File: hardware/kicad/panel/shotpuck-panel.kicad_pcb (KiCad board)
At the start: 2 copper layers, 75 x 91 mm, 237 parts, among them J1_0 Samzo PR5L4015-2P-C-F, J1_1 Samzo PR5L4015-2P-C-F, J1_2 Samzo PR5L4015-2P-C-F, J1_3 Samzo PR5L4015-2P-C-F, J2_0 TC2030-NL, J2_1 TC2030-NL, J2_2 TC2030-NL, J2_3 TC2030-NL, Q1_0 DMN63D8LDW, Q1_1 DMN63D8LDW, Q1_2 DMN63D8LDW, Q1_3 DMN63D8LDW, Q2_0 DMN2004DWK, Q2_1 DMN2004DWK, Q2_2 DMN2004DWK, Q2_3 DMN2004DWK, U1_0 MDBT50Q-1MV2, U1_1 MDBT50Q-1MV2, U1_2 MDBT50Q-1MV2, U1_3 MDBT50Q-1MV2, U2_0 LSM6DSO32TR, U2_1 LSM6DSO32TR, U2_2 LSM6DSO32TR, U2_3 LSM6DSO32TR, U3_0 MCP73831T-2ACI/OT, U3_1 MCP73831T-2ACI/OT, U3_2 MCP73831T-2ACI/OT, U3_3 MCP73831T-2ACI/OT, U4_0 BQ29700DSER, U4_1 BQ29700DSER, U4_2 BQ29700DSER, U4_3 BQ29700DSER

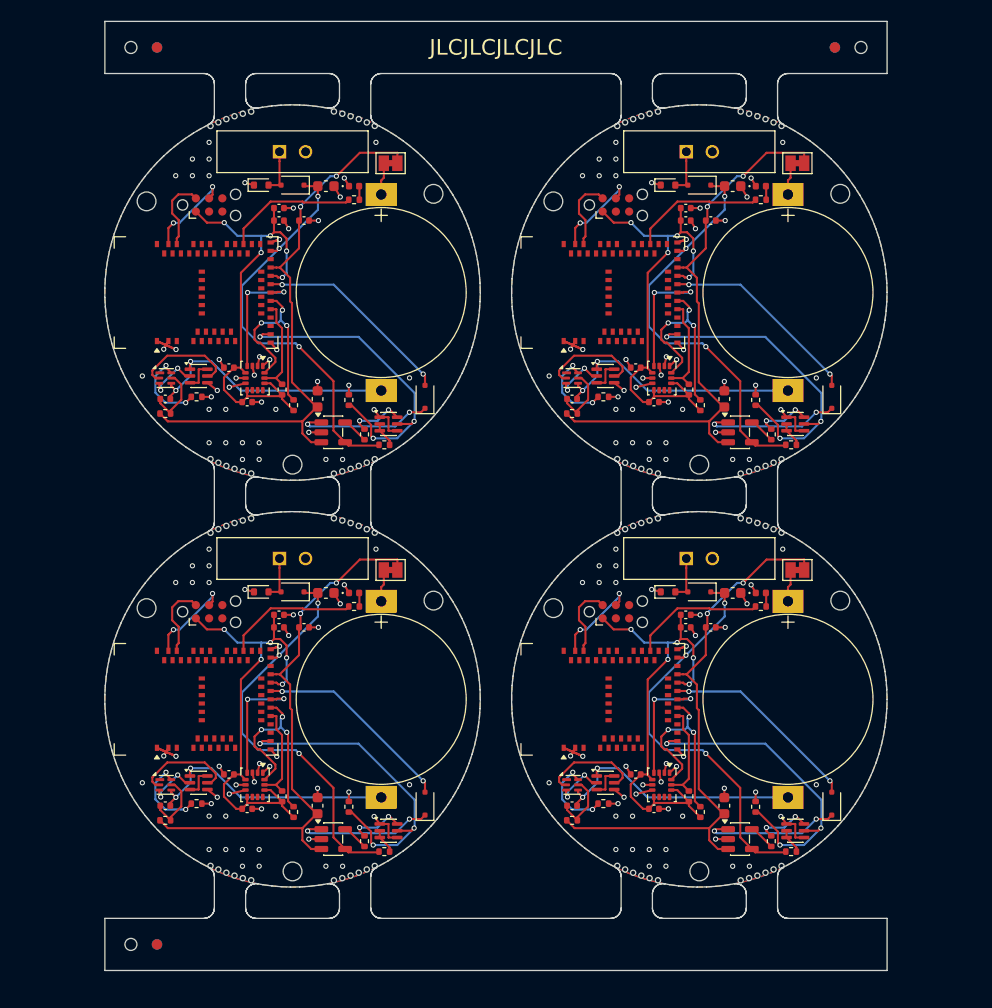
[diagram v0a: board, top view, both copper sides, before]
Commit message: Seat the cell in a PCB notch open to the rim (puck 10.45 mm)
- The cell sits on the Kapton over the base in a notch in the PCB
  (Ø16.6 mm round end, open to the rim) instead of on top of the board,
  saving the 0.8 mm board thickness: 11.25 -> 10.45 mm, 19.8 g with the
  optional brass pins, 18.0 g without.
- Rounded relief on the + side lets the bottom (+ can) tab bend up to the
  + pad; cell pads moved to ±10.2 mm.
- Screw boss 35° -> 40° so its face stays on the board beside the notch;
  JP1 turned upright, D2 moved to the bottom centre (CHG_STAT had no route
  past the notch).
- gen_pcb.py builds the whole outline (rim arc, notch lines, arcs) and a
  copper keep-out along the notch; puck.py cuts the same shape.
- Assembly: full Kapton disc, foam/RTV between cell and cap wall.
- Board DRC 0/0, panel DRC 0/0, netlist PASS; fab, panel and JLC files
  regenerated.

Co-Authored-By: Claude Opus 5.5 <noreply@anthropic.com>
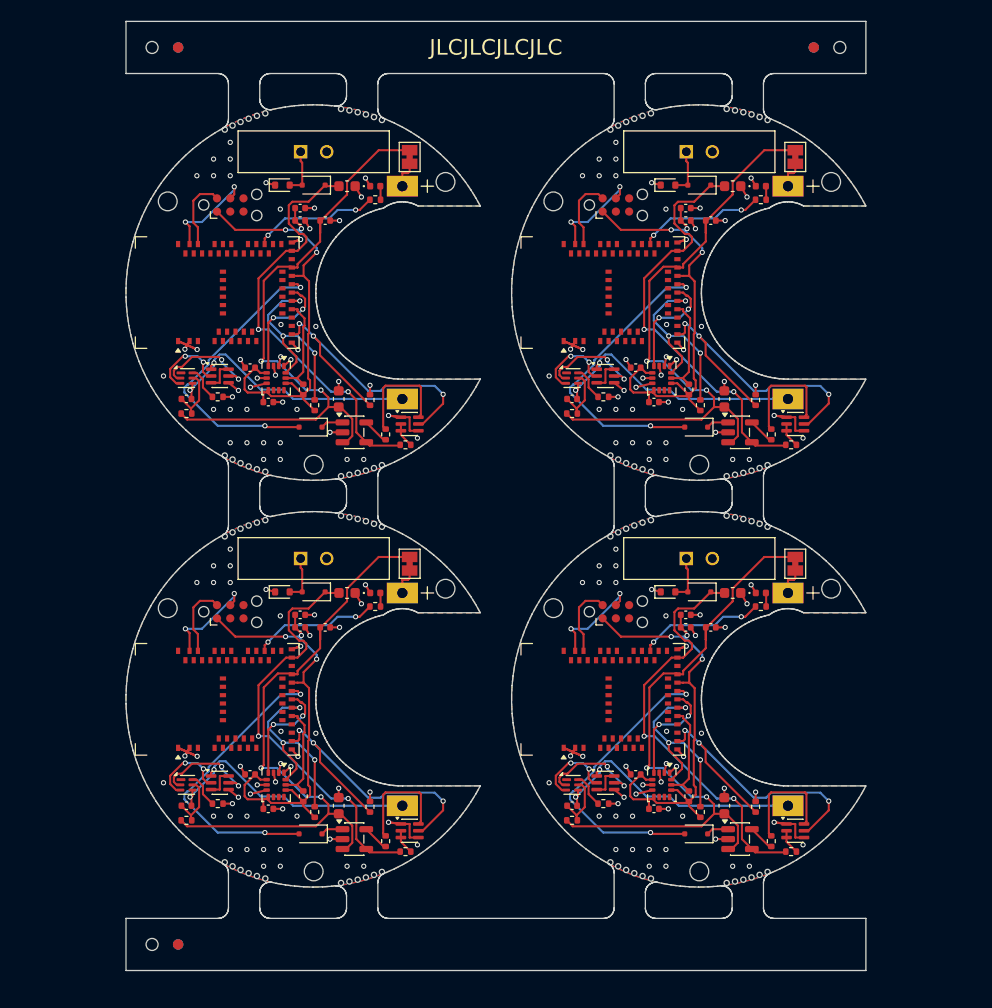
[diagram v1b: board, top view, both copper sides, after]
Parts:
- moved D2_3 13.3 mm to (167.7, 97.9), turned to 180 degrees
- moved D2_1 13.3 mm to (167.7, 58.9), turned to 180 degrees
- moved D2_2 11.3 mm to (130.7, 97.9), turned to 180 degrees
- moved D2_0 11.3 mm to (130.7, 58.9), turned to 180 degrees
- moved KiKit_FID_B_3 2.03 mm to (118.0, 108.5)
- moved KiKit_FID_T_3 2.03 mm to (118.0, 108.5)
- moved KiKit_TO_3 2.03 mm to (115.5, 108.5)
- moved KiKit_FID_B_2 2.03 mm to (179.0, 22.5)
- moved KiKit_FID_T_2 2.03 mm to (179.0, 22.5)
- moved KiKit_TO_2 2.03 mm to (181.5, 22.5)
- moved KiKit_FID_B_1 2.03 mm to (118.0, 22.5)
- moved KiKit_FID_T_1 2.03 mm to (118.0, 22.5)
- moved KiKit_TO_1 2.03 mm to (115.5, 22.5)
- moved BT1_0 2.03 mm to (139.5, 46.0)
- moved BT1_2 2.03 mm to (139.5, 85.0)
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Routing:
- net Board_1-STAT: track 13.4 -> 2.15 mm, vias 2 -> 0
- net Board_0-STAT: track 13.4 -> 2.15 mm, vias 2 -> 0
- net Board_3-STAT: track 13.4 -> 2.15 mm, vias 2 -> 0
- net Board_2-STAT: track 13.4 -> 2.15 mm, vias 2 -> 0
- net Board_3-CHG_STAT: track 19.3 -> 29.2 mm
- net Board_1-CHG_STAT: track 19.3 -> 29.2 mm
- net Board_2-CHG_STAT: track 19.3 -> 29.2 mm
- net Board_0-CHG_STAT: track 19.3 -> 29.2 mm
- net Board_3-PROG_SW: track 5.32 -> 10.8 mm, vias 2 -> 0
- net Board_2-PROG_SW: track 5.32 -> 10.8 mm, vias 2 -> 0
- net Board_1-PROG_SW: track 5.32 -> 10.8 mm, vias 2 -> 0
- net Board_0-PROG_SW: track 5.32 -> 10.8 mm, vias 2 -> 0
- net Board_3-VBAT: track 54.2 -> 59.5 mm
- net Board_1-VBAT: track 54.2 -> 59.5 mm
- net Board_0-VBAT: track 54.2 -> 59.5 mm
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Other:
- board size 75 x 91 mm -> 70.9 x 91 mm

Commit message: Update ShotPuck design to rev A: replace stud with flat plate, adjust dimensions, and enhance PCB layout
- Redesigned the ShotPuck to use a 2.0 mm flat 6061 plate, bolted through a steel sleeve, improving manufacturability and cost.
- Adjusted dimensions: puck height reduced to 9.90 mm, with a center of mass 0.85 mm off-axis.
- Updated layout.json to reflect new design parameters, including cell placement and PCB notch.
- Enhanced mechanical and electrical design files, including updated battery specifications (LIR1254) and revised component placements.
- Improved documentation in HANDOVER.md and README.md to reflect changes in design and functionality.

Co-Authored-By: Claude Opus 5.5 <noreply@anthropic.com>
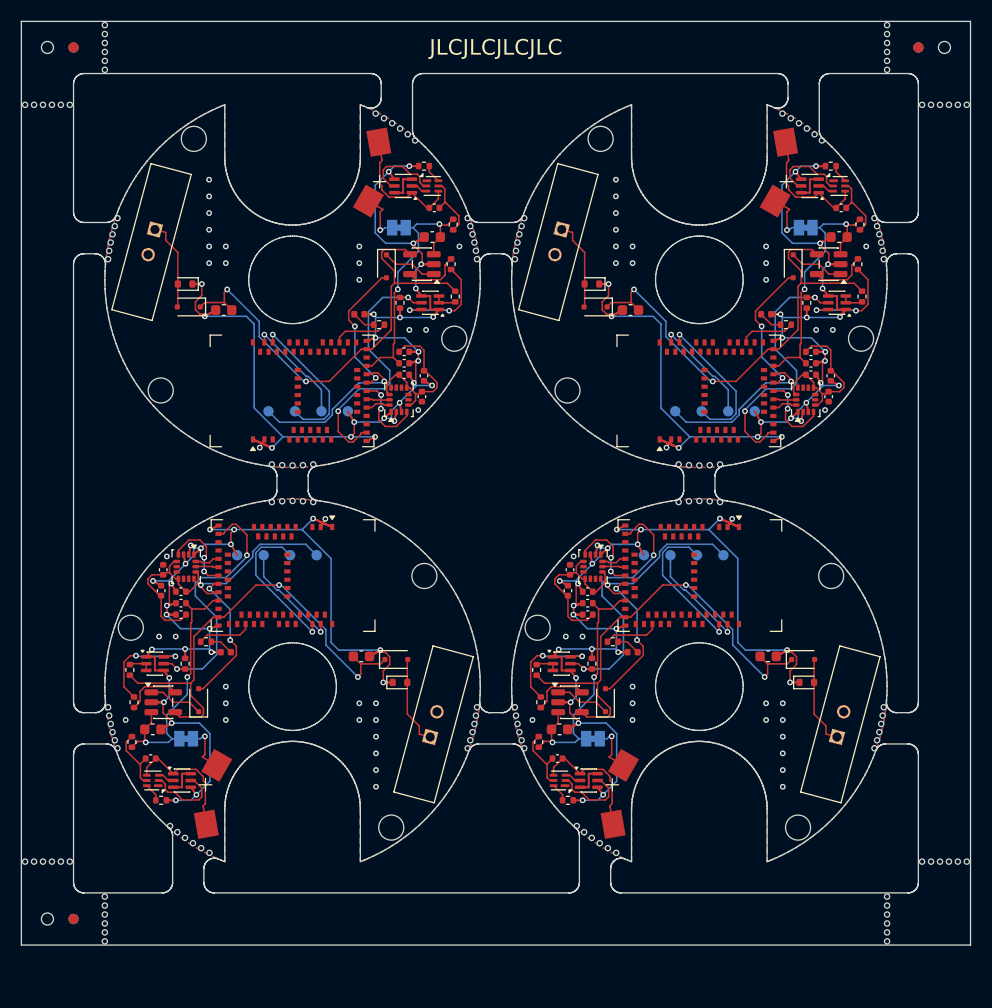
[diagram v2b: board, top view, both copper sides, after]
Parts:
- removed KiKit_MB_10_6, KiKit_MB_14_6, KiKit_MB_2_6, KiKit_MB_6_6: NPTH, NPTH
- removed R5_0, R5_1, R5_2, R5_3, R6_0, R6_1, R6_2, R6_3: 4.7k DNP, Resistor_SMD:R_0402_1005Metric
- added KiKit_MB_17_2: NPTH, NPTH, F.Cu at (111.0, 20.4)
- added KiKit_MB_17_3: NPTH, NPTH, F.Cu at (111.0, 21.2)
- added KiKit_MB_17_4: NPTH, NPTH, F.Cu at (111.0, 22.1)
- added KiKit_MB_17_5: NPTH, NPTH, F.Cu at (111.0, 22.9)
- added KiKit_MB_17_6: NPTH, NPTH, F.Cu at (111.0, 23.8)
- added KiKit_MB_17_7: NPTH, NPTH, F.Cu at (111.0, 24.6)
- added KiKit_MB_18_2: NPTH, NPTH, F.Cu at (186.0, 20.4)
- added KiKit_MB_18_3: NPTH, NPTH, F.Cu at (186.0, 21.2)
- added KiKit_MB_18_4: NPTH, NPTH, F.Cu at (186.0, 22.1)
- added KiKit_MB_18_5: NPTH, NPTH, F.Cu at (186.0, 22.9)
- added KiKit_MB_18_6: NPTH, NPTH, F.Cu at (186.0, 23.8)
- added KiKit_MB_18_7: NPTH, NPTH, F.Cu at (186.0, 24.6)
- added KiKit_MB_19_2: NPTH, NPTH, F.Cu at (111.0, 103.9)
- added KiKit_MB_19_3: NPTH, NPTH, F.Cu at (111.0, 104.8)
- added KiKit_MB_19_4: NPTH, NPTH, F.Cu at (111.0, 105.6)
- added KiKit_MB_19_5: NPTH, NPTH, F.Cu at (111.0, 106.5)
- added KiKit_MB_19_6: NPTH, NPTH, F.Cu at (111.0, 107.3)
- added KiKit_MB_19_7: NPTH, NPTH, F.Cu at (111.0, 108.2)
- added KiKit_MB_20_2: NPTH, NPTH, F.Cu at (186.0, 103.9)
- added KiKit_MB_20_3: NPTH, NPTH, F.Cu at (186.0, 104.8)
- added KiKit_MB_20_4: NPTH, NPTH, F.Cu at (186.0, 105.6)
- added KiKit_MB_20_5: NPTH, NPTH, F.Cu at (186.0, 106.5)
- added KiKit_MB_20_6: NPTH, NPTH, F.Cu at (186.0, 107.3)
- added KiKit_MB_20_7: NPTH, NPTH, F.Cu at (186.0, 108.2)
- added KiKit_MB_21_2: NPTH, NPTH, F.Cu at (103.4, 28.0)
- added KiKit_MB_21_3: NPTH, NPTH, F.Cu at (104.2, 28.0)
- added KiKit_MB_21_4: NPTH, NPTH, F.Cu at (105.1, 28.0)
- added KiKit_MB_21_5: NPTH, NPTH, F.Cu at (105.9, 28.0)
- added KiKit_MB_21_6: NPTH, NPTH, F.Cu at (106.8, 28.0)
- added KiKit_MB_21_7: NPTH, NPTH, F.Cu at (107.6, 28.0)
- added KiKit_MB_22_2: NPTH, NPTH, F.Cu at (103.4, 100.6)
- added KiKit_MB_22_3: NPTH, NPTH, F.Cu at (104.2, 100.6)
- added KiKit_MB_22_4: NPTH, NPTH, F.Cu at (105.1, 100.6)
- added KiKit_MB_22_5: NPTH, NPTH, F.Cu at (105.9, 100.6)
- added KiKit_MB_22_6: NPTH, NPTH, F.Cu at (106.8, 100.6)
- added KiKit_MB_22_7: NPTH, NPTH, F.Cu at (107.6, 100.6)
- added KiKit_MB_23_2: NPTH, NPTH, F.Cu at (189.4, 28.0)
- added KiKit_MB_23_3: NPTH, NPTH, F.Cu at (190.2, 28.0)
- added KiKit_MB_23_4: NPTH, NPTH, F.Cu at (191.1, 28.0)
- added KiKit_MB_23_5: NPTH, NPTH, F.Cu at (191.9, 28.0)
- added KiKit_MB_23_6: NPTH, NPTH, F.Cu at (192.8, 28.0)
- added KiKit_MB_23_7: NPTH, NPTH, F.Cu at (193.6, 28.0)
- added KiKit_MB_24_2: NPTH, NPTH, F.Cu at (189.4, 100.6)
- added KiKit_MB_24_3: NPTH, NPTH, F.Cu at (190.2, 100.6)
- added KiKit_MB_24_4: NPTH, NPTH, F.Cu at (191.1, 100.6)
- added KiKit_MB_24_5: NPTH, NPTH, F.Cu at (191.9, 100.6)
- added KiKit_MB_24_6: NPTH, NPTH, F.Cu at (192.8, 100.6)
- added KiKit_MB_24_7: NPTH, NPTH, F.Cu at (193.6, 100.6)
- BT1_0, BT1_1, BT1_2, BT1_3: value Varta CP1654 A3 (wire or tag version) -> LIR1254 (plain, spring contacts); footprint ShotPuck:CP1654_Pads -> ShotPuck:LIR1254_Contacts
- H1_0, H1_1, H1_2, H1_3, H2_0, H2_1, H2_2, H2_3, H3_0, H3_1, H3_2, H3_3: value M1.6 -> M2; footprint ShotPuck:MountingHole_1.8mm_NPTH -> ShotPuck:MountingHole_2.4mm_NPTH
- J2_0, J2_1, J2_2, J2_3: value TC2030-NL -> SWD pads; footprint Connector:Tag-Connect_TC2030-IDC-NL_2x03_P1.27mm_Vertical -> ShotPuck:SWD_Pads_1x4_P2.54; moved to B.Cu
- JP1_0, JP1_1, JP1_2, JP1_3: moved to B.Cu
- R1_0, R1_1, R1_2, R1_3: value 20k 1% -> 47k 1%
- moved KiKit_MB_2_5 34.7 mm to (127.0, 62.5)
- moved KiKit_MB_2_4 34.6 mm to (128.0, 62.5)
- moved KiKit_MB_2_3 34.4 mm to (129.0, 62.6)
- moved KiKit_MB_2_2 34.3 mm to (130.0, 62.5)
- moved KiKit_MB_6_5 34.2 mm to (166.0, 62.5)
- moved KiKit_MB_2_1 34.2 mm to (131.0, 62.5)
- moved KiKit_MB_6_4 34.2 mm to (167.0, 62.5)
- moved KiKit_MB_6_3 34.1 mm to (168.0, 62.6)
- moved KiKit_MB_6_2 34.1 mm to (169.0, 62.5)
- moved KiKit_MB_6_1 34.1 mm to (170.0, 62.5)
- moved H1_0 33.8 mm to (116.4, 55.4), turned to 180 degrees
- moved H3_0 33.3 mm to (119.5, 31.3), turned to 180 degrees
- moved R7_1 33.0 mm to (183.4, 39.5), turned to -90 degrees
- moved H3_1 32.6 mm to (158.5, 31.3), turned to 180 degrees
- moved H2_1 32.3 mm to (183.5, 50.4), turned to 180 degrees
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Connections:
- J2_0 pad 3: (no net) -> Board_0-SWDCLK
- J2_0 pad 4: Board_0-SWDCLK -> Board_0-GND
- J2_1 pad 3: (no net) -> Board_1-SWDCLK
- J2_1 pad 4: Board_1-SWDCLK -> Board_1-GND
- J2_2 pad 3: (no net) -> Board_2-SWDCLK
- J2_2 pad 4: Board_2-SWDCLK -> Board_2-GND
- J2_3 pad 3: (no net) -> Board_3-SWDCLK
- J2_3 pad 4: Board_3-SWDCLK -> Board_3-GND
- U1_0 pad 20: Board_0-SCL -> Board_0-SDA
- U1_0 pad 22: Board_0-SDA -> Board_0-SCL
- U1_1 pad 20: Board_1-SCL -> Board_1-SDA
- U1_1 pad 22: Board_1-SDA -> Board_1-SCL
- U1_2 pad 20: Board_2-SCL -> Board_2-SDA
- U1_2 pad 22: Board_2-SDA -> Board_2-SCL
- U1_3 pad 20: Board_3-SCL -> Board_3-SDA
- U1_3 pad 22: Board_3-SDA -> Board_3-SCL
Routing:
- net Board_1-GND: track 31.7 -> 109.5 mm, vias 46 -> 38
- net Board_3-GND: track 31.7 -> 109.5 mm, vias 46 -> 38
- net Board_2-GND: track 31.7 -> 109.5 mm, vias 46 -> 38
- net Board_0-GND: track 31.7 -> 109.5 mm, vias 46 -> 38
- net Board_3-VBAT: track 59.5 -> 25.4 mm
- net Board_1-VBAT: track 59.5 -> 25.4 mm
- net Board_0-VBAT: track 59.5 -> 25.4 mm
- net Board_2-VBAT: track 59.5 -> 25.4 mm
- net Board_3-SDA: track 19.7 -> 2.39 mm, vias 3 -> 0
- net Board_1-SDA: track 19.7 -> 2.39 mm, vias 3 -> 0
- net Board_2-SDA: track 19.7 -> 2.39 mm, vias 3 -> 0
- net Board_0-SDA: track 19.7 -> 2.39 mm, vias 3 -> 0
- net Board_3-CHG_STAT: track 29.2 -> 13.5 mm
- net Board_1-CHG_STAT: track 29.2 -> 13.5 mm
- net Board_0-CHG_STAT: track 29.2 -> 13.5 mm
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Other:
- board size 70.9 x 91 mm -> 91 x 88.6 mm

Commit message: Refine ShotPuck design and documentation for improved functionality and clarity
- Updated `HANDOVER.md` to clarify PCB routing and placement procedures, emphasizing the importance of running `gen_pcb.py --no-route` and `global_route.py` for optimal results.
- Revised `README.md` to correct the center of mass measurement and enhance the description of the puck's dimensions.
- Enhanced `VALIDATION.md` to reflect updated weight and balance metrics, ensuring accurate representation of the ShotPuck's specifications.
- Adjusted `design.py` to include new charge-input protection details and updated component specifications for better clarity.
- Improved `gen_bom.py` and `gen_jlc.py` to reflect changes in component sourcing and specifications.

Co-Authored-By: Claude Opus 5.5 <noreply@anthropic.com>
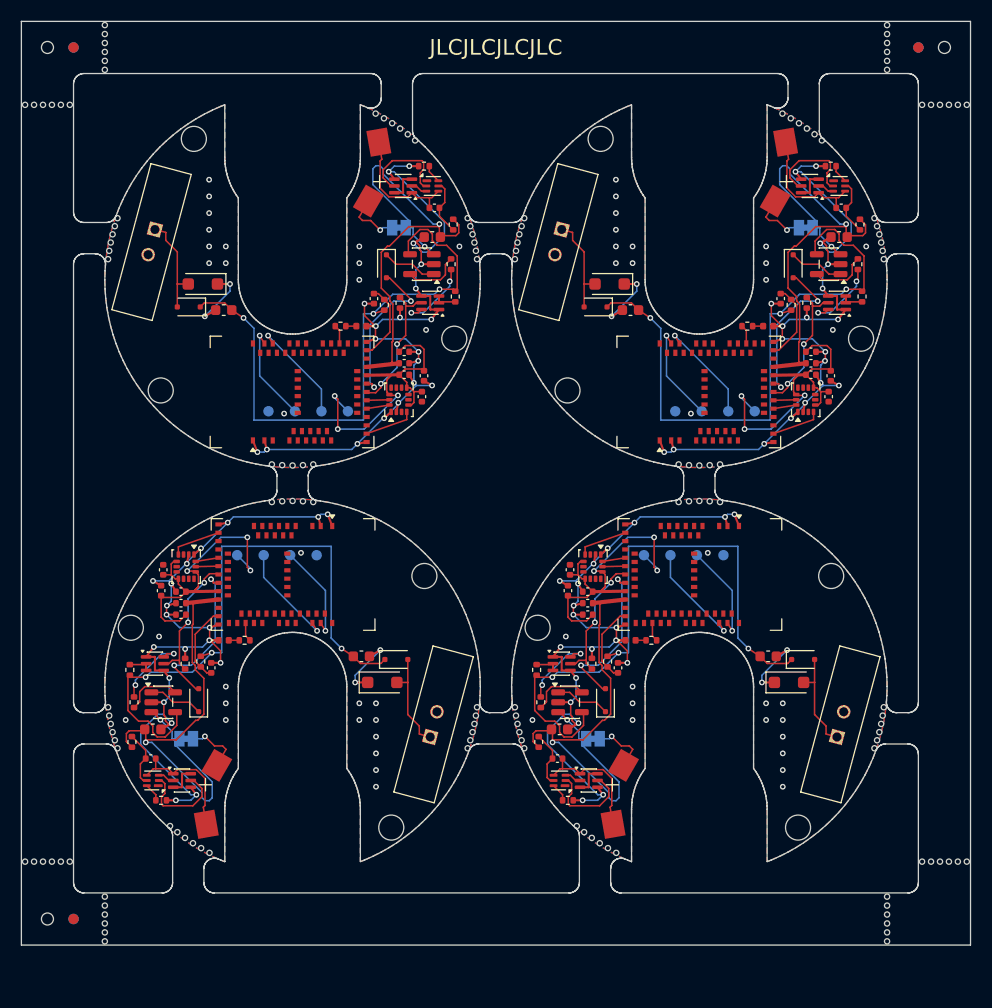
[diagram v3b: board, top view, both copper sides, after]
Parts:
- added C9_0: 100n, Capacitor_SMD:C_0402_1005Metric, F.Cu at (136.8, 46.6)
- added C9_1: 100n, Capacitor_SMD:C_0402_1005Metric, F.Cu at (175.8, 46.6)
- added C9_2: 100n, Capacitor_SMD:C_0402_1005Metric, F.Cu at (121.2, 82.0)
- added C9_3: 100n, Capacitor_SMD:C_0402_1005Metric, F.Cu at (160.2, 82.0)
- added R9_0: 1k, Resistor_SMD:R_0402_1005Metric, F.Cu at (137.8, 47.2)
- added R9_1: 1k, Resistor_SMD:R_0402_1005Metric, F.Cu at (176.8, 47.2)
- added R9_2: 1k, Resistor_SMD:R_0402_1005Metric, F.Cu at (120.2, 81.4)
- added R9_3: 1k, Resistor_SMD:R_0402_1005Metric, F.Cu at (159.2, 81.4)
- C2_0, C2_1, C2_2, C2_3: value 4.7u 10V -> 10u 10V
- D3_0, D3_1, D3_2, D3_3: value PESD5V0S1BB -> SMF5.0CA; footprint Diode_SMD:D_SOD-523 -> Diode_SMD:D_SOD-123F
- D4_0, D4_1, D4_2, D4_3: value LED green 0402 -> LED yellow-green 0402
- moved KiKit_MB_15_3 34.7 mm to (150.7, 88.1)
- moved KiKit_MB_15_4 34.7 mm to (150.6, 87.4)
- moved KiKit_MB_16_3 34.7 mm to (185.4, 87.4)
- moved KiKit_MB_16_4 34.7 mm to (185.3, 88.1)
- moved KiKit_MB_7_3 34.7 mm to (185.3, 40.4)
- moved KiKit_MB_7_4 34.7 mm to (185.4, 41.2)
- moved KiKit_MB_8_3 34.7 mm to (150.6, 41.2)
- moved KiKit_MB_8_4 34.7 mm to (150.7, 40.4)
- moved KiKit_MB_11_3 34.7 mm to (111.7, 88.1)
- moved KiKit_MB_11_4 34.7 mm to (111.6, 87.4)
- moved KiKit_MB_12_3 34.7 mm to (146.4, 87.4)
- moved KiKit_MB_12_4 34.7 mm to (146.3, 88.1)
- moved KiKit_MB_3_3 34.7 mm to (146.3, 40.4)
- moved KiKit_MB_3_4 34.7 mm to (146.4, 41.2)
- moved KiKit_MB_4_3 34.7 mm to (111.6, 41.2)
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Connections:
- U1_0 pad 16: Board_0-CHG_INH -> Board_0-ACC_INT1
- U1_0 pad 24: Board_0-ACC_INT1 -> Board_0-CHG_INH
- U1_0 pad 32: Board_0-VIN -> Board_0-VBUS_SNS
- U1_1 pad 16: Board_1-CHG_INH -> Board_1-ACC_INT1
- U1_1 pad 24: Board_1-ACC_INT1 -> Board_1-CHG_INH
- U1_1 pad 32: Board_1-VIN -> Board_1-VBUS_SNS
- U1_2 pad 16: Board_2-CHG_INH -> Board_2-ACC_INT1
- U1_2 pad 24: Board_2-ACC_INT1 -> Board_2-CHG_INH
- U1_2 pad 32: Board_2-VIN -> Board_2-VBUS_SNS
- U1_3 pad 16: Board_3-CHG_INH -> Board_3-ACC_INT1
- U1_3 pad 24: Board_3-ACC_INT1 -> Board_3-CHG_INH
- U1_3 pad 32: Board_3-VIN -> Board_3-VBUS_SNS
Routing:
- net Board_1-GND: track 109.5 -> 86.8 mm, vias 38 -> 35
- net Board_3-GND: track 109.5 -> 86.8 mm, vias 38 -> 35
- net Board_0-GND: track 109.5 -> 86.8 mm, vias 38 -> 35
- net Board_2-GND: track 109.5 -> 86.8 mm, vias 38 -> 35
- net Board_3-VBAT: track 25.4 -> 46.7 mm
- net Board_0-VBAT: track 25.4 -> 46.7 mm
- net Board_1-VBAT: track 25.4 -> 46.7 mm
- net Board_2-VBAT: track 25.4 -> 46.7 mm
- net Board_0-VIN: track 44.4 -> 58.1 mm, vias 2 -> 3
- net Board_2-VIN: track 44.4 -> 58.1 mm, vias 2 -> 3
- net Board_1-VIN: track 44.4 -> 58.1 mm, vias 2 -> 3
- net Board_3-VIN: track 44.4 -> 58.1 mm, vias 2 -> 3
- net Board_3-CHG_INH: track 26.0 -> 13.1 mm
- net Board_2-CHG_INH: track 26.0 -> 13.1 mm
- net Board_1-CHG_INH: track 26.0 -> 13.1 mm
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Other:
- outline, holes or cut-outs redrawn
